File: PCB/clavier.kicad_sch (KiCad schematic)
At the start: 0 parts

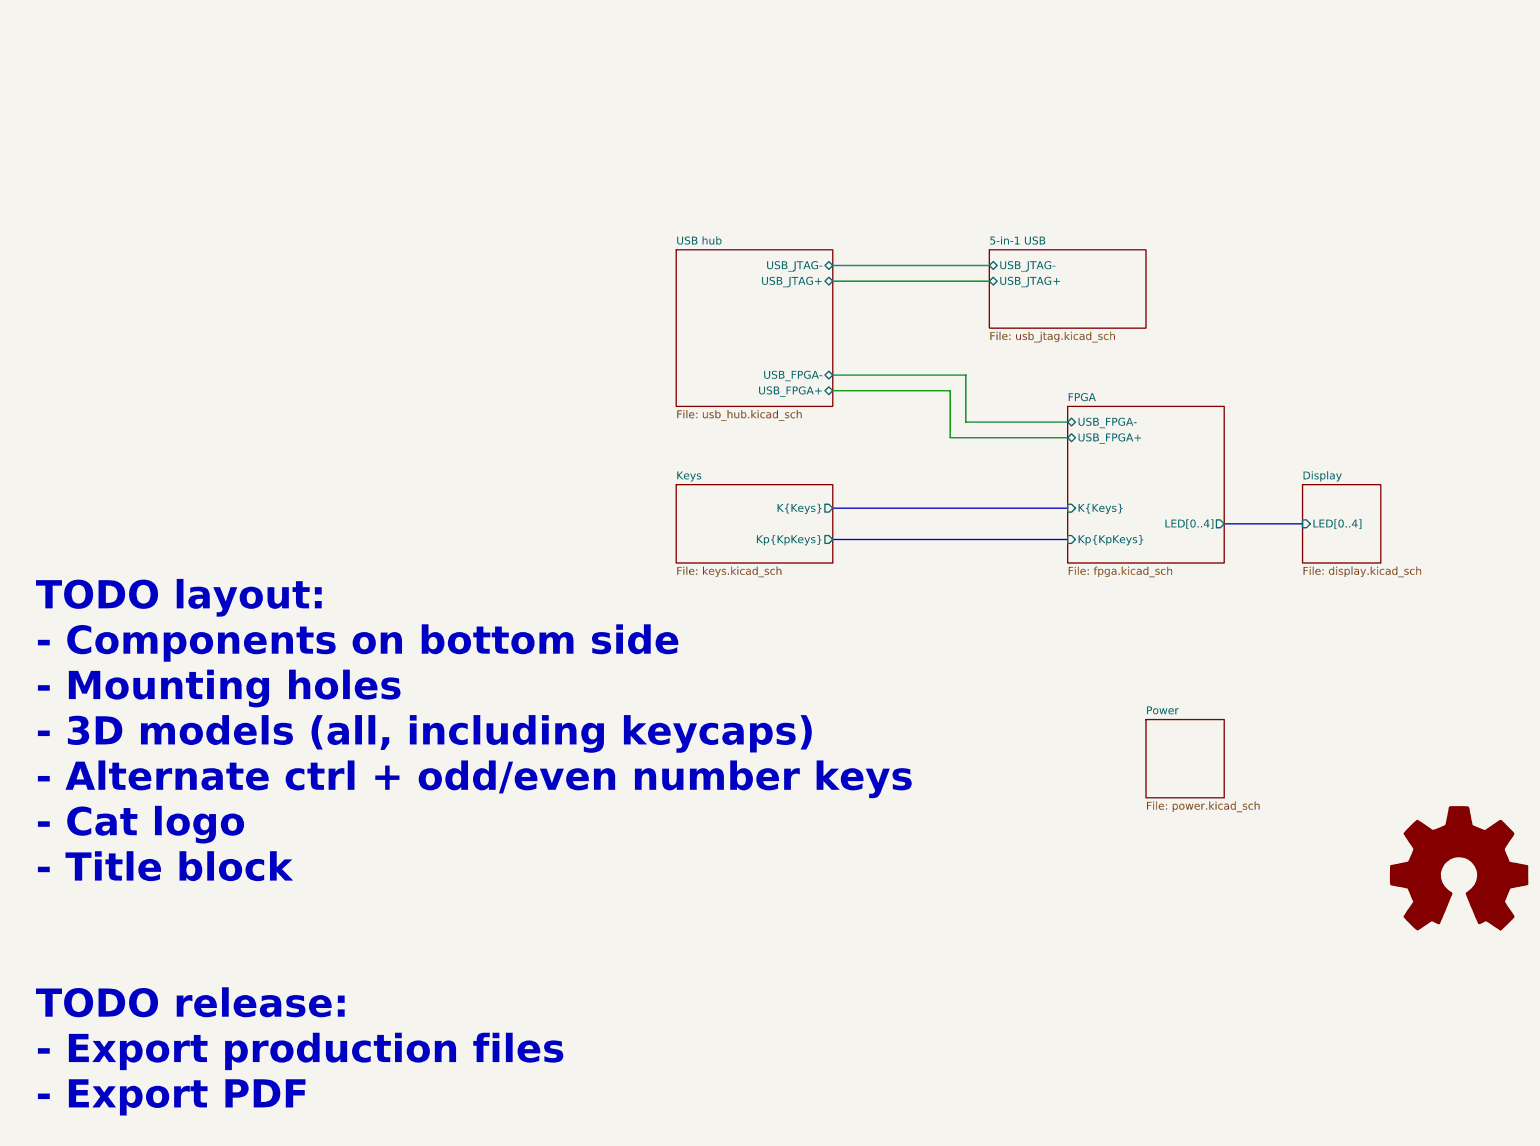
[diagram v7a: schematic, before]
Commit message: Add more keycaps
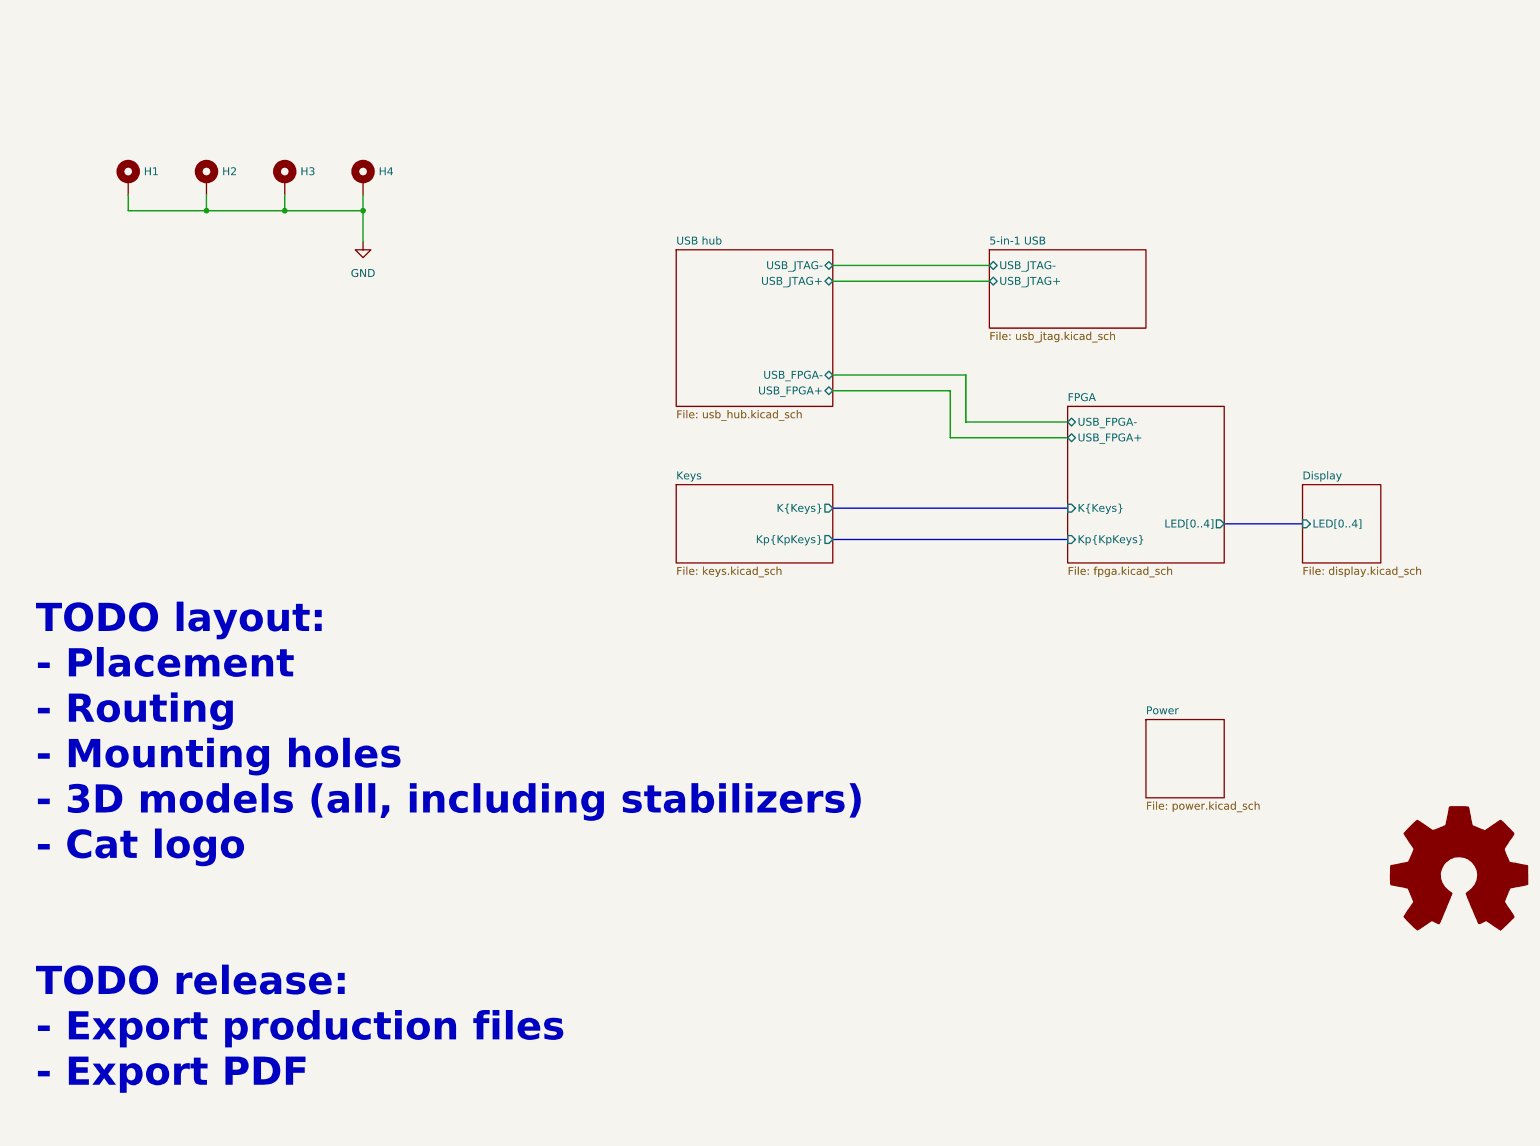
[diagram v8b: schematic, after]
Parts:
- added H1, H2, H3, H4: MountingHole_Pad, MountingHole:MountingHole_3.2mm_M3_ISO7380_Pad_TopBottom, symbol Mechanical:MountingHole_Pad
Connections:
- new net GND: H1.1, H2.1, H3.1, H4.1
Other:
- note added: "TODO layout: - Placement - Routing - Mounting holes - 3D models (all, including stabilizers) - Cat logo TODO release: - Export production files - Export PDF"
- note removed: "TODO layout: - Components on bottom side - Mounting holes - 3D models (all, including keycaps) - Alternate ctrl + odd/even number keys - Cat logo - Title block TODO release: - Export production files - Export PDF"
